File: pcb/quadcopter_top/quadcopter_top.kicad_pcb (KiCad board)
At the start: 2 copper layers, 48.3 x 73.7 mm, 14 parts, among them IC1 ATMEGA328P-A, J1 RJ45

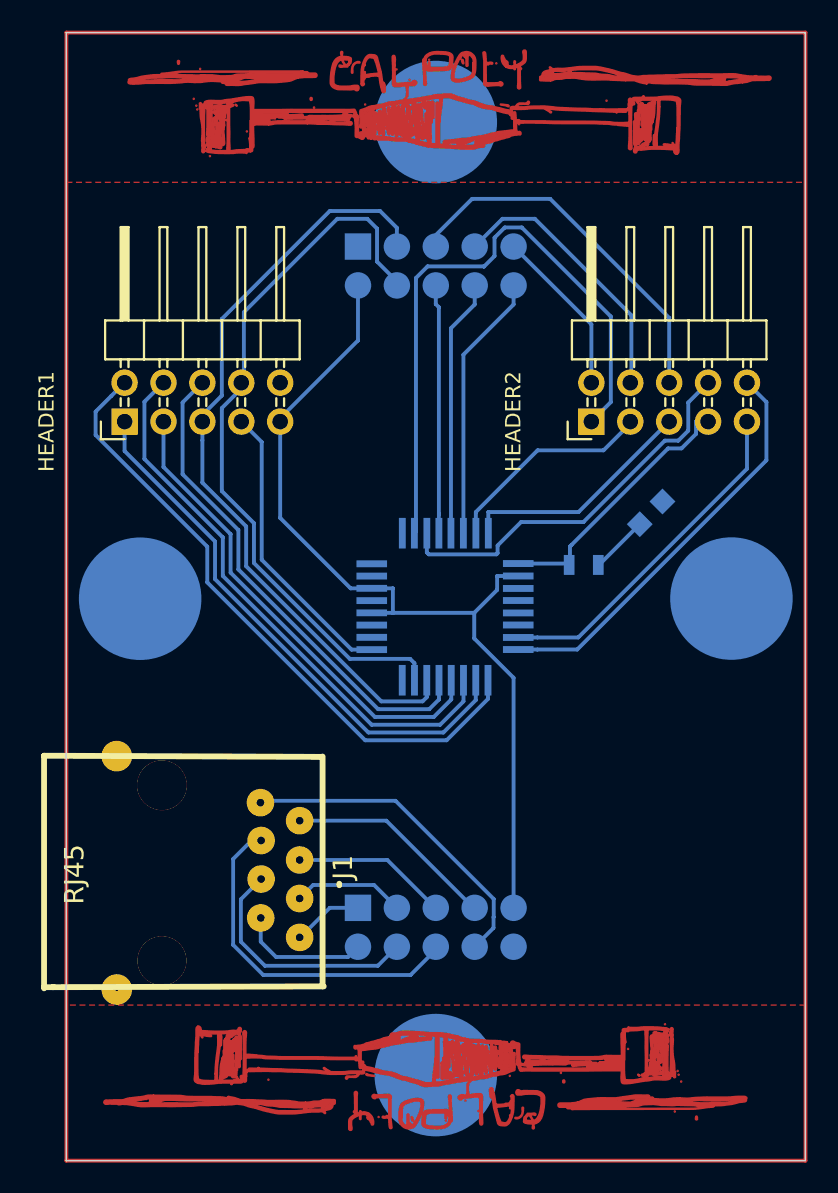
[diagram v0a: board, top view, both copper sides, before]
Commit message: fixed silkscreen, added mounting holes, added 3D models
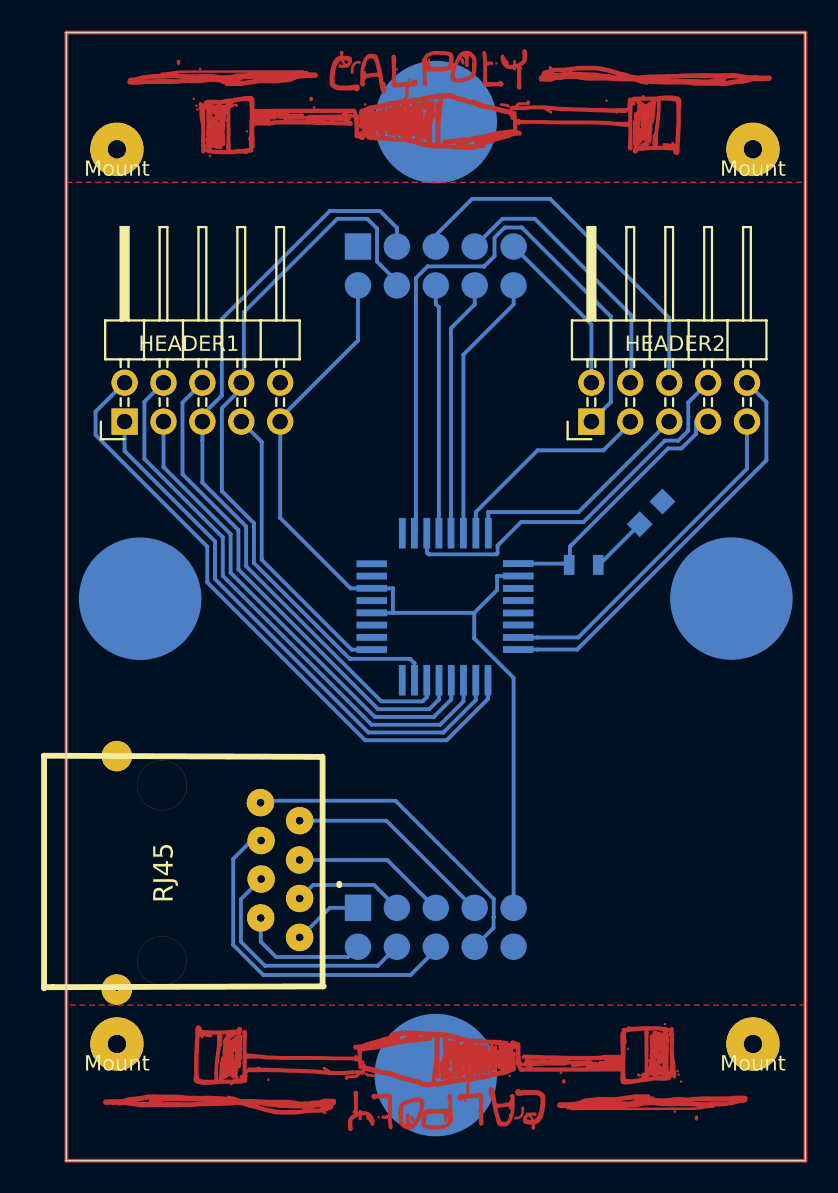
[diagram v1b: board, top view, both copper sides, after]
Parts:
- added Mount: Mount, Wire_Pads:SolderWirePad_single_1-2mmDrill, F.Cu at (245.1, 115.6)
- added Mount: Mount, Wire_Pads:SolderWirePad_single_1-2mmDrill, F.Cu at (203.6, 115.6)
- added Mount: Mount, Wire_Pads:SolderWirePad_single_1-2mmDrill, F.Cu at (203.6, 57.1)
- added Mount: Mount, Wire_Pads:SolderWirePad_single_1-2mmDrill, F.Cu at (245.1, 57.1)
- renumbered IC1 to 328P, D1 to LED
